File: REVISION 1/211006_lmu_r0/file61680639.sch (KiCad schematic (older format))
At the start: 18 parts

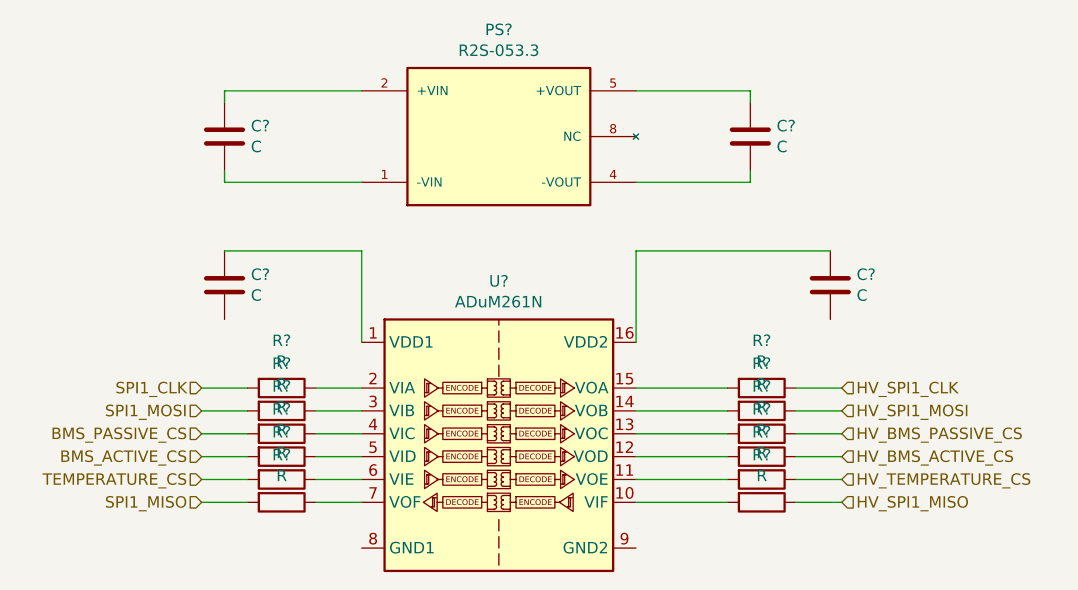
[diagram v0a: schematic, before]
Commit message: Added new a-balancer interface
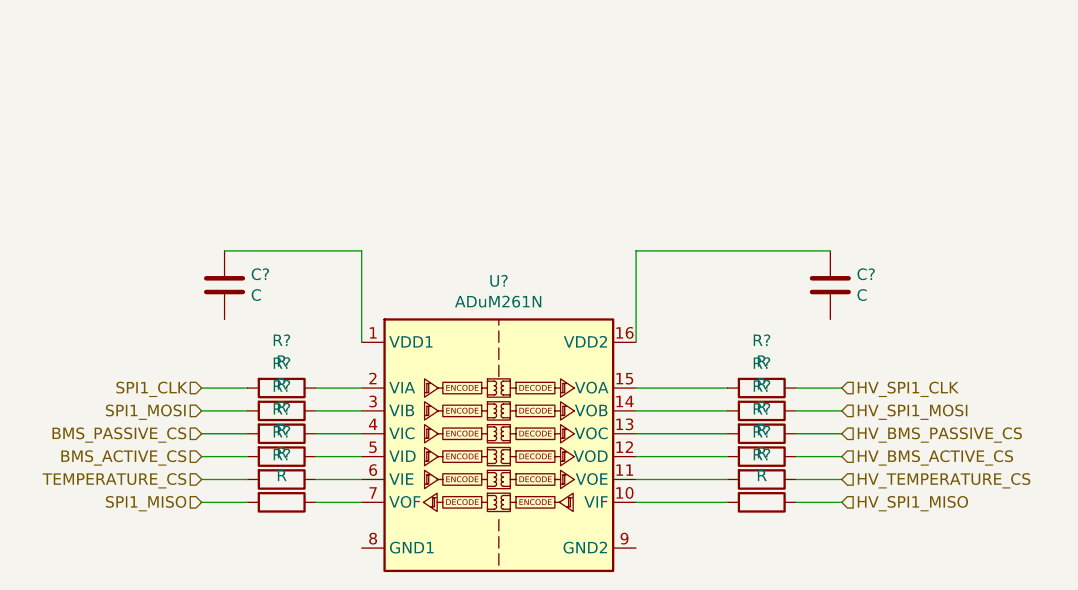
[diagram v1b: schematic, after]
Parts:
- removed C? (x2): C, symbol Device:C
- removed PS?: R2S-053.3, CONV_R2S-053.3, symbol R2S-053.3:R2S-053.3
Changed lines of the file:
@@
 $Descr A4 11693 8268
 encoding utf-8
-Sheet 5 7
+Sheet 5 30
 Title ""
 Date ""
@@
 $Comp
 L Device:C C?
-U 1 1 61688002
-P 6750 3050
-F 0 "C?" H 6865 3096 50  0000 L CNN
-F 1 "C" H 6865 3005 50  0000 L CNN
-F 2 "" H 6788 2900 50  0001 C CNN
-F 3 "~" H 6750 3050 50  0001 C CNN
-	1    6750 3050
-	1    0    0    -1
-$EndComp
-$Comp
-L Device:C C?
-U 1 1 616886EA
-P 4450 3050
-F 0 "C?" H 4565 3096 50  0000 L CNN
-F 1 "C" H 4565 3005 50  0000 L CNN
-F 2 "" H 4488 2900 50  0001 C CNN
-F 3 "~" H 4450 3050 50  0001 C CNN
-	1    4450 3050
-	1    0    0    -1
-$EndComp
-Wire Wire Line
-	4450 2900 4450 2850
-$Comp
-L R2S-053.3:R2S-053.3 PS?
-U 1 1 6168971C
-P 5650 3050
-F 0 "PS?" H 5650 3517 50  0000 C CNN
-F 1 "R2S-053.3" H 5650 3426 50  0000 C CNN
-F 2 "CONV_R2S-053.3" H 5650 3050 50  0001 L BNN
-F 3 "" H 5650 3050 50  0001 L BNN
-F 4 "RECOM" H 5650 3050 50  0001 L BNN "MANUFACTURER"
-F 5 "9.0mm" H 5650 3050 50  0001 L BNN "MAXIMUM_PACKAGE_HEIGHT"
-F 6 "Manufacturer Recommendations" H 5650 3050 50  0001 L BNN "STANDARD"
-F 7 "0" H 5650 3050 50  0001 L BNN "PARTREV"
-	1    5650 3050
-	1    0    0    -1
-$EndComp
-Wire Wire Line
-	4450 2850 5050 2850
-Wire Wire Line
-	5050 3250 4450 3250
-Wire Wire Line
-	4450 3250 4450 3200
-Wire Wire Line
-	6250 3250 6750 3250
-Wire Wire Line
-	6750 3250 6750 3200
-Wire Wire Line
-	6750 2900 6750 2850
-Wire Wire Line
-	6750 2850 6250 2850
-$Comp
-L Device:C C?
